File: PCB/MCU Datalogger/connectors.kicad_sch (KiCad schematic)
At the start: 4 parts, among them J1 Conn_01x04_Pin, J2 Conn_01x04_Pin, J3 Conn_01x09_Pin, J4 Conn_02x03_Odd_Even

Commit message: Associate
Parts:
- J1, J2: footprint (none) -> Connector_PinHeader_2.54mm:PinHeader_1x04_P2.54mm_Vertical
- J3: footprint (none) -> Connector_PinHeader_2.54mm:PinHeader_1x09_P2.54mm_Vertical
- J4: footprint (none) -> Connector_PinHeader_2.54mm:PinHeader_2x03_P2.54mm_Vertical
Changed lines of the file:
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@@
       (effects (font (size 1.27 1.27)))
     )
-    (property "Footprint" "" (at 69.85 43.18 0)
+    (property "Footprint" "Connector_PinHeader_2.54mm:PinHeader_1x04_P2.54mm_Vertical" (at 69.85 43.18 0)
       (effects (font (size 1.27 1.27)) hide)
     )
@@
       (effects (font (size 1.27 1.27)))
     )
-    (property "Footprint" "" (at 50.8 78.74 0)
+    (property "Footprint" "Connector_PinHeader_2.54mm:PinHeader_1x09_P2.54mm_Vertical" (at 50.8 78.74 0)
       (effects (font (size 1.27 1.27)) hide)
     )
@@
       (effects (font (size 1.27 1.27)))
     )
-    (property "Footprint" "" (at 73.66 77.47 0)
+    (property "Footprint" "Connector_PinHeader_2.54mm:PinHeader_2x03_P2.54mm_Vertical" (at 73.66 77.47 0)
       (effects (font (size 1.27 1.27)) hide)
     )
@@
       (effects (font (size 1.27 1.27)))
     )
-    (property "Footprint" "" (at 50.8 43.18 0)
+    (property "Footprint" "Connector_PinHeader_2.54mm:PinHeader_1x04_P2.54mm_Vertical" (at 50.8 43.18 0)
       (effects (font (size 1.27 1.27)) hide)
     )

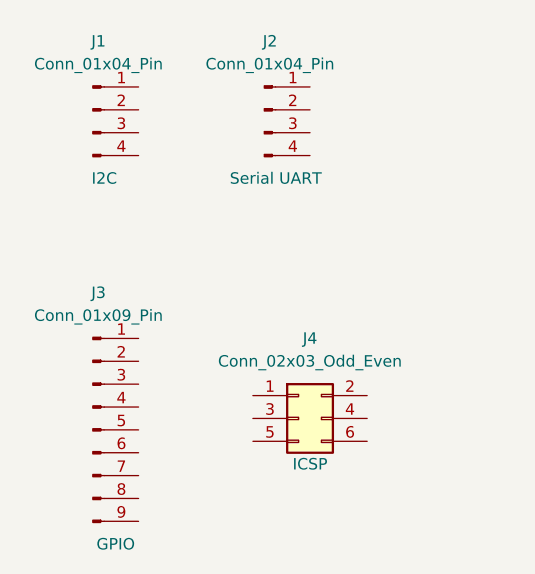
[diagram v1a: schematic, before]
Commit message: Wiring of sheet 2
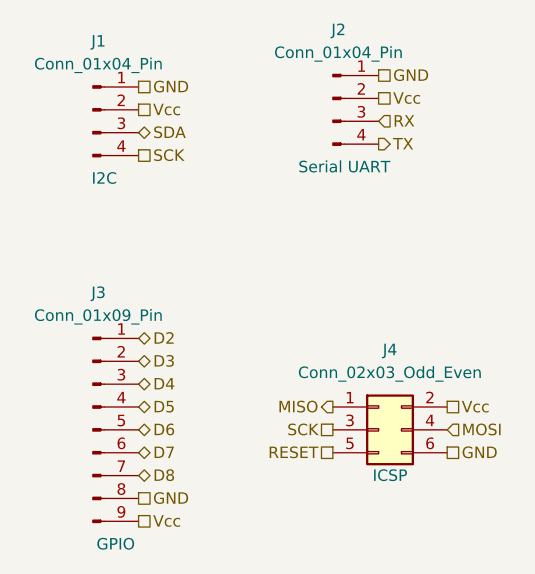
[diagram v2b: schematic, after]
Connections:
- net GND: now reaches J2.1 (Pin_1)
- net GND: now also J1.1 (Pin_1), J3.8 (Pin_8), J4.6 (Pin_6)
- net Vcc: now reaches J2.2 (Pin_2)
- net Vcc: now also J1.2 (Pin_2), J3.9 (Pin_9), J4.2 (Pin_2)
- net RX: now reaches J2.3 (Pin_3)
- net TX: now reaches J2.4 (Pin_4)
- net D2: now reaches J3.1 (Pin_1)
- net D3: now reaches J3.2 (Pin_2)
- net D4: now reaches J3.3 (Pin_3)
- net D5: now reaches J3.4 (Pin_4)
- net D6: now reaches J3.5 (Pin_5)
- net D7: now reaches J3.6 (Pin_6)
- net D8: now reaches J3.7 (Pin_7)
- net MISO: now reaches J4.1 (Pin_1)
- net SCK: now reaches J4.3 (Pin_3)
- net SCK: now also J1.4 (Pin_4)
- net MOSI: now reaches J4.4 (Pin_4)
- net RESET: now reaches J4.5 (Pin_5)
- net SDA: now reaches J1.3 (Pin_3)
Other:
- moved on the sheet: J2, J4
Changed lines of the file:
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@@
 (kicad_sch (version 20230121) (generator eeschema)
   (paper "A4")
-  (symbol (lib_id "Connector:Conn_01x04_Pin") (at 69.85 43.18 0) (unit 1)
+  (hierarchical_label "D4" (shape bidirectional) (at 55.88 73.66 0) (fields_autoplaced)
+    (effects (font (size 1.27 1.27)) (justify left))
+  )
+  (hierarchical_label "GND" (shape passive) (at 55.88 86.36 0) (fields_autoplaced)
+    (effects (font (size 1.27 1.27)) (justify left))
+  )
+  (hierarchical_label "D5" (shape bidirectional) (at 55.88 76.2 0) (fields_autoplaced)
+    (effects (font (size 1.27 1.27)) (justify left))
+  )
+  (hierarchical_label "GND" (shape passive) (at 55.88 40.64 0) (fields_autoplaced)
+    (effects (font (size 1.27 1.27)) (justify left))
+  )
+  (hierarchical_label "Vcc" (shape passive) (at 90.17 76.2 0) (fields_autoplaced)
+    (effects (font (size 1.27 1.27)) (justify left))
+  )
+  (hierarchical_label "Vcc" (shape passive) (at 82.55 41.91 0) (fields_autoplaced)
+    (effects (font (size 1.27 1.27)) (justify left))
+  )
+  (hierarchical_label "Vcc" (shape passive) (at 55.88 43.18 0) (fields_autoplaced)
+    (effects (font (size 1.27 1.27)) (justify left))
+  )
+  (hierarchical_label "SCK" (shape passive) (at 55.88 48.26 0) (fields_autoplaced)
+    (effects (font (size 1.27 1.27)) (justify left))
+  )
+  (hierarchical_label "D3" (shape bidirectional) (at 55.88 71.12 0) (fields_autoplaced)
+    (effects (font (size 1.27 1.27)) (justify left))
+  )
+  (hierarchical_label "D7" (shape bidirectional) (at 55.88 81.28 0) (fields_autoplaced)
+    (effects (font (size 1.27 1.27)) (justify left))
+  )
+  (hierarchical_label "D6" (shape bidirectional) (at 55.88 78.74 0) (fields_autoplaced)
+    (effects (font (size 1.27 1.27)) (justify left))
+  )
+  (hierarchical_label "MISO" (shape output) (at 77.47 76.2 180) (fields_autoplaced)
+    (effects (font (size 1.27 1.27)) (justify right))
+  )
+  (hierarchical_label "SCK" (shape passive) (at 77.47 78.74 180) (fields_autoplaced)
+    (effects (font (size 1.27 1.27)) (justify right))
+  )
+  (hierarchical_label "RX" (shape input) (at 82.55 44.45 0) (fields_autoplaced)
+    (effects (font (size 1.27 1.27)) (justify left))
+  )
+  (hierarchical_label "GND" (shape passive) (at 90.17 81.28 0) (fields_autoplaced)
+    (effects (font (size 1.27 1.27)) (justify left))
+  )
+  (hierarchical_label "D8" (shape bidirectional) (at 55.88 83.82 0) (fields_autoplaced)
+    (effects (font (size 1.27 1.27)) (justify left))
+  )
+  (hierarchical_label "D2" (shape bidirectional) (at 55.88 68.58 0) (fields_autoplaced)
+    (effects (font (size 1.27 1.27)) (justify left))
+  )
+  (hierarchical_label "MOSI" (shape input) (at 90.17 78.74 0) (fields_autoplaced)
+    (effects (font (size 1.27 1.27)) (justify left))
+  )
+  (hierarchical_label "SDA" (shape bidirectional) (at 55.88 45.72 0) (fields_autoplaced)
+    (effects (font (size 1.27 1.27)) (justify left))
+  )
+  (hierarchical_label "GND" (shape passive) (at 82.55 39.37 0) (fields_autoplaced)
+    (effects (font (size 1.27 1.27)) (justify left))
+  )
+  (hierarchical_label "RESET" (shape passive) (at 77.47 81.28 180) (fields_autoplaced)
+    (effects (font (size 1.27 1.27)) (justify right))
+  )
+  (hierarchical_label "TX" (shape output) (at 82.55 46.99 0) (fields_autoplaced)
+    (effects (font (size 1.27 1.27)) (justify left))
+  )
+  (hierarchical_label "Vcc" (shape passive) (at 55.88 88.9 0) (fields_autoplaced)
+    (effects (font (size 1.27 1.27)) (justify left))
+  )
+  (symbol (lib_id "Connector:Conn_01x04_Pin") (at 77.47 41.91 0) (unit 1)
     (in_bom yes) (on_board yes) (dnp no)
-    (property "Reference" "J2" (at 70.485 35.56 0)
+    (property "Reference" "J2" (at 78.105 34.29 0)
       (effects (font (size 1.27 1.27)))
     )
-    (property "Value" "Conn_01x04_Pin" (at 70.485 38.1 0)
+    (property "Value" "Conn_01x04_Pin" (at 78.105 36.83 0)
       (effects (font (size 1.27 1.27)))
     )
-    (property "Footprint" "Connector_PinHeader_2.54mm:PinHeader_1x04_P2.54mm_Vertical" (at 69.85 43.18 0)
+    (property "Footprint" "Connector_PinHeader_2.54mm:PinHeader_1x04_P2.54mm_Vertical" (at 77.47 41.91 0)
       (effects (font (size 1.27 1.27)) hide)
     )
-    (property "Datasheet" "~" (at 69.85 43.18 0)
+    (property "Datasheet" "~" (at 77.47 41.91 0)
       (effects (font (size 1.27 1.27)) hide)
     )
-    (property "Purpose" "Serial UART" (at 71.12 50.8 0)
+    (property "Purpose" "Serial UART" (at 78.74 49.53 0)
       (effects (font (size 1.27 1.27)))
     )
@@
     )
   )
-  (symbol (lib_id "Connector_Generic:Conn_02x03_Odd_Even") (at 73.66 77.47 0) (unit 1)
+  (symbol (lib_id "Connector_Generic:Conn_02x03_Odd_Even") (at 82.55 78.74 0) (unit 1)
     (in_bom yes) (on_board yes) (dnp no)
-    (property "Reference" "J4" (at 74.93 68.58 0)
+    (property "Reference" "J4" (at 83.82 69.85 0)
       (effects (font (size 1.27 1.27)))
     )
-    (property "Value" "Conn_02x03_Odd_Even" (at 74.93 71.12 0)
+    (property "Value" "Conn_02x03_Odd_Even" (at 83.82 72.39 0)
       (effects (font (size 1.27 1.27)))
     )
-    (property "Footprint" "Connector_PinHeader_2.54mm:PinHeader_2x03_P2.54mm_Vertical" (at 73.66 77.47 0)
+    (property "Footprint" "Connector_PinHeader_2.54mm:PinHeader_2x03_P2.54mm_Vertical" (at 82.55 78.74 0)
       (effects (font (size 1.27 1.27)) hide)
     )
-    (property "Datasheet" "~" (at 73.66 77.47 0)
+    (property "Datasheet" "~" (at 82.55 78.74 0)
       (effects (font (size 1.27 1.27)) hide)
     )
-    (property "Purpose" "ICSP" (at 74.93 82.55 0)
+    (property "Purpose" "ICSP" (at 83.82 83.82 0)
       (effects (font (size 1.27 1.27)))
     )
